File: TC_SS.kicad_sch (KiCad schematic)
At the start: 36 parts, among them Q1 IPW60R099P6XKSA1, Q2 IPW60R099P6XKSA1, Q3 IPW60R099P6XKSA1, Q4 IPW60R099P6XKSA1, U1 IR2184, U2 IR2184

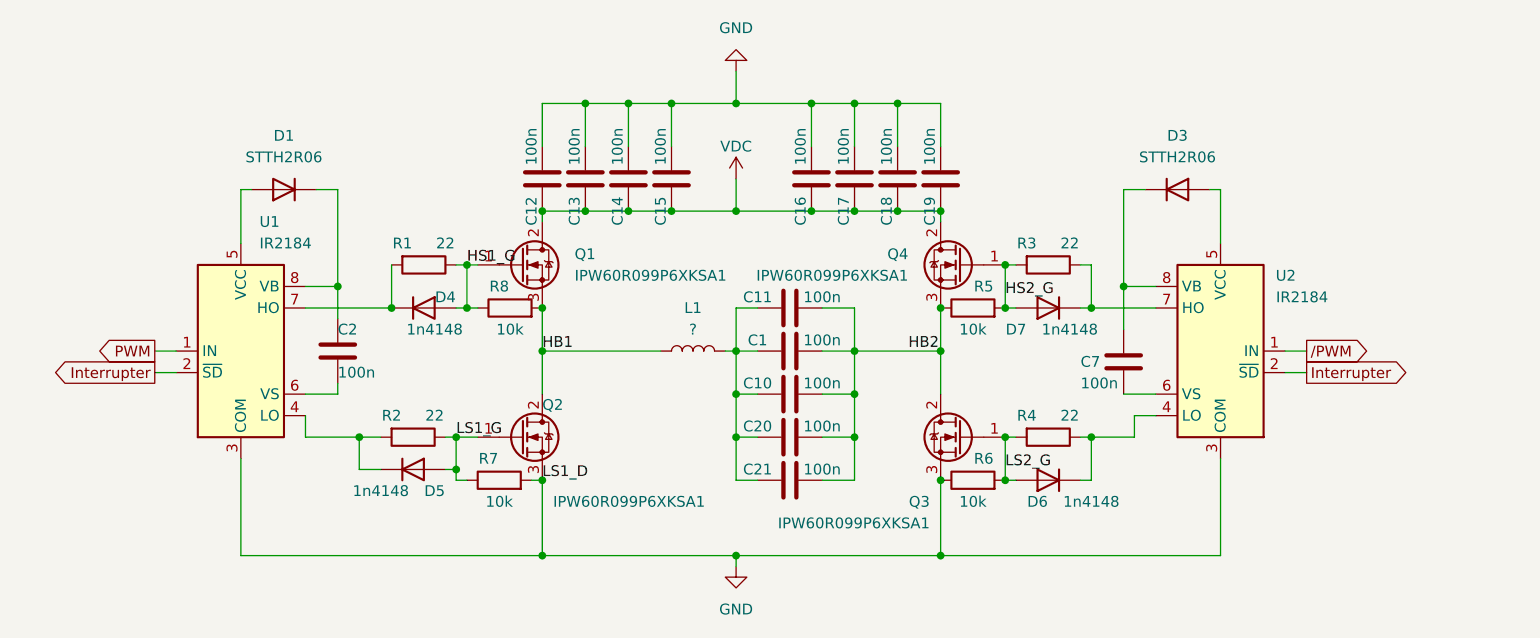
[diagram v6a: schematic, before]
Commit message: Swap gate driver for Adum4221-1
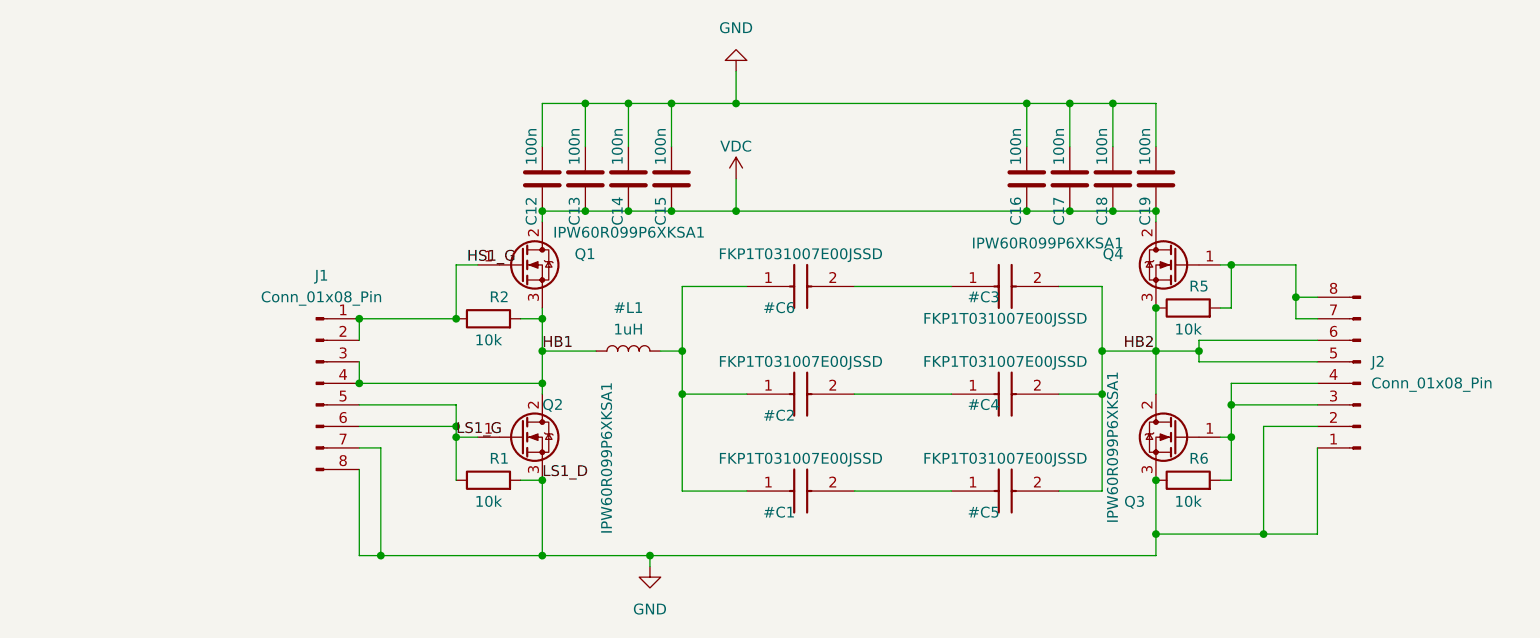
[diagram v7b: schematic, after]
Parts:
- removed C1, C10, C11, C20, C21: 100n, Capacitor_SMD:C_2220_5650Metric, symbol Device:C
- removed C2, C7: 100n, Capacitor_SMD:C_0805_2012Metric_Pad1.18x1.45mm_HandSolder, symbol Device:C
- removed D1, D3: STTH2R06, Diode_SMD:D_SMB, symbol Device:D
- removed D4, D5, D6, D7: 1n4148, Diode_SMD:D_SMB, symbol Device:D
- removed R3, R4: 22, Resistor_SMD:R_1206_3216Metric_Pad1.30x1.75mm_HandSolder, symbol Device:R
- removed R7, R8: 10k, Resistor_SMD:R_1206_3216Metric_Pad1.30x1.75mm_HandSolder, symbol Device:R
- removed U1, U2: IR2184, Package_DIP:DIP-8_W7.62mm_Socket, symbol Driver_FET:IR2184
- added #C1, #C2, #C3, #C4, #C5, #C6: FKP1T031007E00JSSD, symbol:FKP1T031007E00JSSD, symbol FKP1T031007E00JSSD:FKP1T031007E00JSSD
- added J1, J2: Conn_01x08_Pin, Connector_PinHeader_2.54mm:PinHeader_1x08_P2.54mm_Vertical, symbol Connector:Conn_01x08_Pin
- #L1: renamed from L1; value ? -> 1uH
- R1, R2: value 22 -> 10k
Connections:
- net GND: now also R1.2, J1.7 (Pin_7), J1.8 (Pin_8), J2.1 (Pin_1), J2.2 (Pin_2)
- net HB1: now also R2.2, J1.3 (Pin_3), J1.4 (Pin_4)
- net HB2: now also #C3.2, #C4.2, #C5.2, J2.5 (Pin_5), J2.6 (Pin_6)
- net HS1_G: now also R2.1, J1.1 (Pin_1), J1.2 (Pin_2); no longer R1.1
- net LS1_G: now also R1.1, J1.5 (Pin_5), J1.6 (Pin_6); no longer R2.1
- net at #L1.2: now also #C1.1, #C2.1, #C6.1
- net HS2_G: no longer names the net of Q4.1 (G), R5.2
- net HS2_G: now also J2.7 (Pin_7), J2.8 (Pin_8)
- net LS2_G: no longer names the net of Q3.1 (G), R6.2
- net LS2_G: now also J2.3 (Pin_3), J2.4 (Pin_4)
- new net: #C1.2, #C5.1
- new net: #C2.2, #C4.1
- new net: #C3.1, #C6.2
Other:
- moved on the sheet: C16, C17, C18, C19, Q3, Q4, R5, R6

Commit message: Update basically everything
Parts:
- removed J1, J2: Conn_01x08_Pin, Connector_PinHeader_2.54mm:PinHeader_1x08_P2.54mm_Vertical, symbol Connector:Conn_01x08_Pin
- added #T1: Transformer_1P_1S, symbol Device:Transformer_1P_1S
- added C1, C10, C11, C2, C4, C5, C6, C7, C8, C9: 1u, Capacitor_SMD:C_0805_2012Metric, symbol Device:C_Small
- added C3: 100n, Capacitor_SMD:C_2220_5650Metric, symbol Device:C
- added D1, D4, D5, D6: D, PCM_Diode_SMD_AKL:D_PowerDI-123, symbol Device:D
- added D2, D3: 1N4148WT, Diode_SMD:D_SOD-523, symbol Diode:1N4148WT
- added IC1, IC2: ADUM4221-1ARIZ, SamacSys_Parts:SOIC127P1030X264-16N, symbol SamacSys_Parts:ADUM4221-1ARIZ
- added J1: 15V_In, Connector_PinHeader_2.54mm:PinHeader_1x02_P2.54mm_Vertical, symbol Connector_Generic:Conn_01x02
- added PS1, PS2, PS3, PS4: RKZ-1215S_H, symbol:RKZ1215SH, symbol SamacSys_Parts:RKZ-1215S_H
- added R10: 100, Resistor_SMD:R_0805_2012Metric, symbol Device:R
- added R11, R9: 4.7, Resistor_SMD:R_0805_2012Metric, symbol Device:R_Small
- added R3, R4: 10k, Resistor_SMD:R_0805_2012Metric, symbol Device:R
- added R7, R8: 22, Resistor_SMD:R_0805_2012Metric, symbol Device:R
- added U1: LM7805_TO220, Package_TO_SOT_THT:TO-220-3_Vertical, symbol Regulator_Linear:LM7805_TO220
- added U2: 74HC14, symbol 74xx:74HC14
- added U3: LM7812_TO220, Package_TO_SOT_THT:TO-220-3_Vertical, symbol Regulator_Linear:LM7812_TO220
- R1, R2, R5, R6: footprint Resistor_SMD:R_1206_3216Metric_Pad1.30x1.75mm_HandSolder -> Resistor_SMD:R_0805_2012Metric
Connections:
- net GND: now also C1.2, C10.2, C11.2, C2.2, C4.2, C5.2, C6.2, C7.2, C8.2, C9.2, IC1.4 (GND1), J1.1 (Pin_1), PS1.2 (-VIN), PS2.2 (-VIN), PS2.6 (NO_PIN), PS4.2 (-VIN), PS4.6 (NO_PIN), R11.2, R3.1, R9.1, U1.2 (GND), U2.7 (GND), U3.2 (GND); no longer R6.1
- net HB1: now also PS1.6 (NO_PIN)
- net HB2: now also R4.1; no longer R5.1
- net HS1_G: now also R5.2, D6.1 (K)
- net LS1_G: now also R6.2, D5.1 (K)
- net at Q4.1 (G): now also D4.2 (A), R4.2, R8.1; no longer R5.2
- net at Q3.1 (G): now also D1.2 (A), R3.2, R7.1; no longer R6.2
- new net: #T1.4 (SB), R10.1
- new net: C3.2, R10.2
- new net: D4.1 (K), IC2.10 (VOB), R8.2
- new net: D5.2 (A), IC1.10 (VOB), R6.1
- new net: D6.2 (A), IC1.15 (VOA), R5.1
- new net: IC1.6 (DT), R9.2
- new net: C3.1, D2.2 (A), D3.1 (K), U2.1
- new net: D1.1 (K), IC2.15 (VOA), R7.2
- new net: U2.2, U2.3
- new net: IC2.6 (DT), R11.1
- new net: C10.1, J1.2 (Pin_2), U3.1 (VI)
- new net: #T1.3 (SA), D3.2 (A)
- new net: #T1.1 (AA), #T1.2 (AB)
- new net +12V: C11.1, C4.1, PS1.1 (+VIN), PS2.1 (+VIN), PS4.1 (+VIN), U1.1 (VI), U3.3 (VO)
- new net +5V: C1.1, C2.1, C5.1, C6.1, C7.1, C8.1, C9.1, D2.1 (K), IC1.3 (VDD1_1), IC1.8 (VDD1_2), IC2.3 (VDD1_1), IC2.8 (VDD1_2), U1.3 (VO), U2.11, U2.13, U2.14 (VCC), U2.5, U2.9
- new net PWM: IC1.1 (PWM), IC2.1 (PWM), U2.4
- new net Vg_neg_HS1: IC1.14 (GNDA), PS1.5 (-VOUT)
- new net Vg_neg_HS2: IC2.9 (GNDB)
- new net Vg_neg_LS1: IC1.9 (GNDB), PS2.5 (-VOUT)
- new net Vg_neg_LS2: IC2.14 (GNDA), PS4.5 (-VOUT)
- new net Vg_pos_HS1: IC1.16 (VDDA), PS1.7 (+VOUT)
- new net Vg_pos_HS2: IC2.11 (VDDB)
- new net Vg_pos_LS1: IC1.11 (VDDB), PS2.7 (+VOUT)
- new net Vg_pos_LS2: IC2.16 (VDDA), PS4.7 (+VOUT)
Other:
- moved on the sheet: Q2, R2
